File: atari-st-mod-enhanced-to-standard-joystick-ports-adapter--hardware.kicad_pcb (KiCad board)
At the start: 4 copper layers, 100 x 100 mm, 52 parts, among them J1 Joy0/Mouse, J2 Joy1, J3 OLED 128×64, J4 Enhanced Joystick Port, J5 Joy0/Mouse, J6 Joy1, Q1 1<Vgsth<2, Low Rdson, Vds >10, Q10 1<Vgsth<2, Low Rdson, Vds >10, Q2 1<Vgsth<2, Low Rdson, Vds >10, Q3 1<Vgsth<2, Low Rdson, Vds >10, Q4 1<Vgsth<2, Low Rdson, Vds >10, Q5 1<Vgsth<2, Low Rdson, Vds >10, Q6 1<Vgsth<2, Low Rdson, Vds >10, Q7 1<Vgsth<2, Low Rdson, Vds >10, Q8 1<Vgsth<2, Low Rdson, Vds >10, Q9 1<Vgsth<2, Low Rdson, Vds >10, SW1 Reset, SW2 Selector, SW3 Activate/Change, SW4 Cancel, U1 LM4040DBZ-3

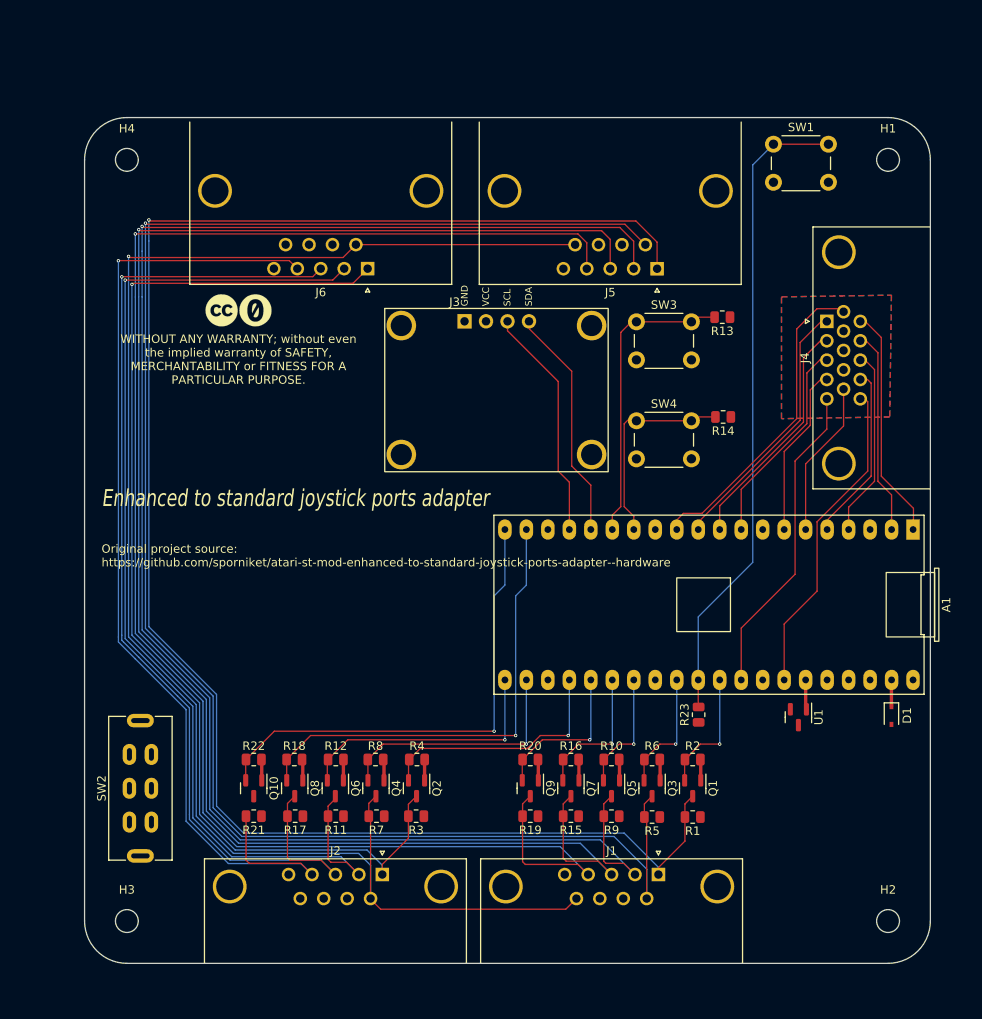
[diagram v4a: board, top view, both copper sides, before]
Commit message: cleaning the trace pathes
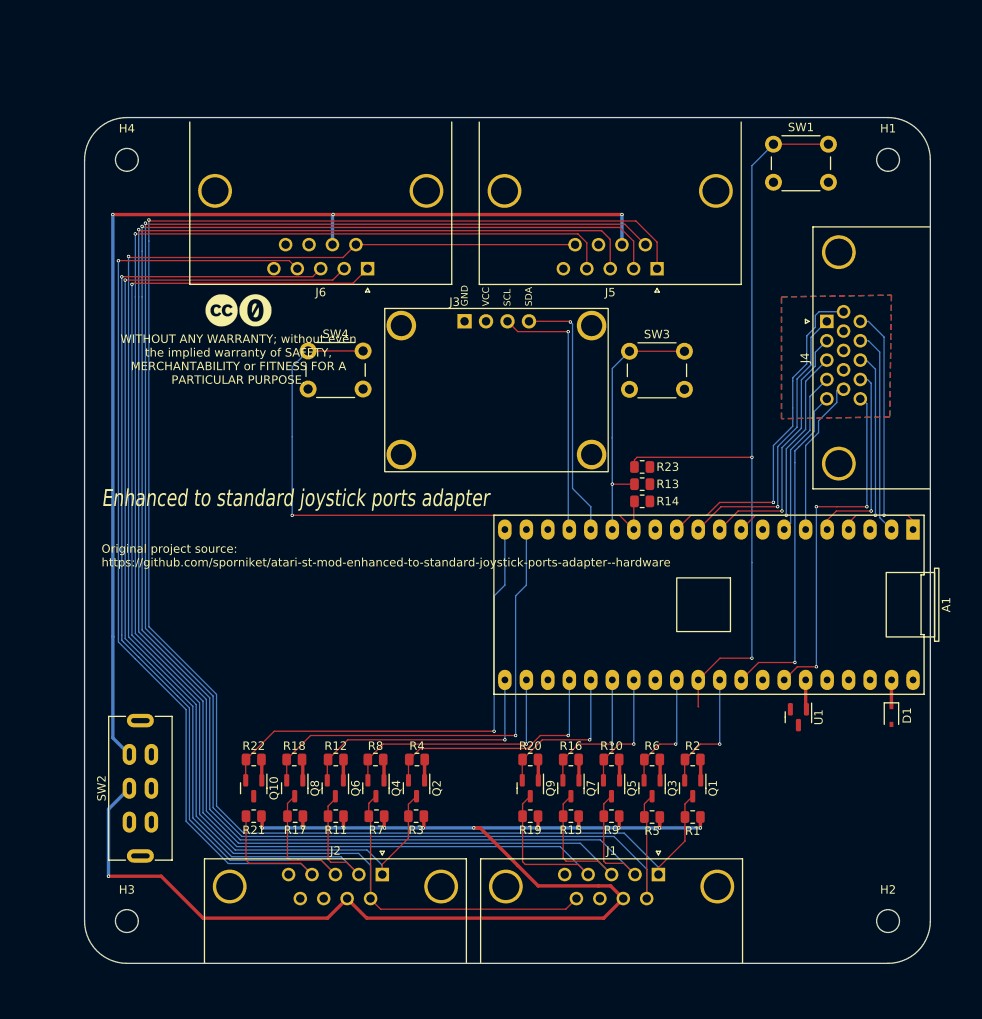
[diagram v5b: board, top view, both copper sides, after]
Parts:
- moved SW4 39.7 mm to (76.4, 77.6)
- moved R23 30.0 mm to (115.9, 91.3), turned to 180 degrees
- moved R13 21.9 mm to (115.9, 93.3)
- moved R14 13.8 mm to (115.9, 95.4)
- moved SW3 3.58 mm to (114.4, 77.6)
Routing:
- net +5V: track 0.00 -> 164.0 mm, vias 0 -> 12
- net +5VA: track 0.00 -> 132.0 mm, vias 0 -> 3
- net /button2: track 24.1 -> 71.2 mm, vias 0 -> 1
- net /reset: track 76.7 -> 93.8 mm, vias 0 -> 2
- net /paddle_x: track 38.0 -> 42.5 mm, vias 0 -> 3
- net /button1: track 35.6 -> 31.1 mm, vias 0 -> 1
- net /jag_col1: track 31.3 -> 35.7 mm, vias 0 -> 1
- net /oled_scl: track 27.6 -> 31.1 mm, vias 0 -> 1
- net /jag_row1: track 37.6 -> 40.4 mm, vias 0 -> 1
- net /oled_sda: track 27.6 -> 30.5 mm, vias 0 -> 1
- net /jag_col2: track 28.0 -> 30.6 mm, vias 0 -> 1
- net /paddle_y: track 37.4 -> 39.9 mm, vias 0 -> 1
- net /jag_row6: track 20.9 -> 23.3 mm, vias 0 -> 1
- net /jag_row3: track 27.6 -> 29.5 mm, vias 0 -> 1
- net /jag_row5: track 22.3 -> 24.0 mm, vias 0 -> 1
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
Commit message: done cleaning
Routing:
- net +3V3: track 24.8 -> 226.9 mm, vias 0 -> 16
- net VCC: track 0.00 -> 120.1 mm, vias 0 -> 3
- net GND1: track 0.00 -> 92.1 mm, vias 0 -> 2
- net /reset: track 93.8 -> 90.6 mm
- net GND2: vias 0 -> 30
- added copper zone on B.Cu, net GND
- added copper zone on F.Cu, net GND
- added copper zone on In1.Cu, net GND
- added copper zone on In2.Cu, net GND
- added copper zone on B.Cu, net GND1
- added copper zone on F.Cu, net GND1
- added copper zone on B.Cu, net GND2
- added copper zone on F.Cu, net GND2
- added copper zone on In1.Cu, net GND2
- added copper zone on In2.Cu, net GND2
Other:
- board text added: "3V3"
- board text added: "5V"
